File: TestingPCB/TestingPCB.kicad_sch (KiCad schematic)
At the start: 19 parts, among them J1 Conn_01x04, J2 USB_C_Receptacle_USB2.0_14P, J4 Conn_01x10, U1 SC0915, U2 CP2102N-Axx-xQFN24, U3 USBLC6-2P6

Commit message: Updated to use the 20 pin package and fixed power for CP2102N
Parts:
- removed U2: CP2102N-Axx-xQFN24, Package_DFN_QFN:QFN-24-1EP_4x4mm_P0.5mm_EP2.6x2.6mm, symbol Interface_USB:CP2102N-Axx-xQFN24
- added U4: CP2102N-Axx-xQFN20, Package_DFN_QFN:SiliconLabs_QFN-20-1EP_3x3mm_P0.5mm_EP1.8x1.8mm, symbol Interface_USB:CP2102N-Axx-xQFN20
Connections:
- net 3.3V: no longer C3.1, C4.1, R5.1
- net D_N: now also U4.5 (D-)
- net D_P: now also U4.4 (D+)
- net GND: now also U4.12 (GND), U4.21 (GND), U4.3 (GND)
- net RX: now also U4.18 (TXD)
- net TX: now also U4.17 (RXD)
- net USB 5V: now also U4.7 (VREGIN)
- net at R3.2, R4.1: now also U4.8 (VBUS)
- net at R5.2: now also U4.9 (~{RST})
- new net VDD: C3.1, C4.1, R5.1, U4.6 (VDD)
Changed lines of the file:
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@@
 	(title_block
 		(title "Thesis PCB")
-		(date "2025-03-09")
+		(date "2025-03-10")
 		(rev "v1.0")
 		(company "Lafayette College Electrical & Computer Engineering Department")
@@
 	)
 	(junction
-		(at 85.09 100.33)
-		(diameter 0)
-		(color 0 0 0 0)
-	)
-	(junction
 		(at 73.66 31.75)
 		(diameter 0)
@@
 	)
 	(junction
+		(at 83.82 93.98)
+		(diameter 0)
+		(color 0 0 0 0)
+	)
+	(junction
 		(at 119.38 81.28)
 		(diameter 0)
@@
 	(wire
 		(pts
-			(xy 83.82 104.14) (xy 83.82 100.33)
-		)
-		(stroke
-			(width 0)
-			(type default)
-		)
-	)
-	(wire
-		(pts
 			(xy 259.08 125.73) (xy 259.08 123.19)
 		)
@@
 	(wire
 		(pts
-			(xy 85.09 100.33) (xy 86.36 100.33)
+			(xy 83.82 93.98) (xy 115.57 93.98)
 		)
 		(stroke
@@
 	(wire
 		(pts
-			(xy 85.09 93.98) (xy 85.09 100.33)
-		)
-		(stroke
-			(width 0)
-			(type default)
-		)
-	)
-	(wire
-		(pts
 			(xy 132.08 115.57) (xy 132.08 106.68)
 		)
@@
 	(wire
 		(pts
-			(xy 86.36 100.33) (xy 86.36 104.14)
-		)
-		(stroke
-			(width 0)
-			(type default)
-		)
-	)
-	(wire
-		(pts
 			(xy 115.57 93.98) (xy 115.57 99.06)
 		)
@@
 	(wire
 		(pts
-			(xy 83.82 100.33) (xy 85.09 100.33)
-		)
-		(stroke
-			(width 0)
-			(type default)
-		)
-	)
-	(wire
-		(pts
 			(xy 156.21 46.99) (xy 165.1 46.99)
 		)
@@
 	(wire
 		(pts
+			(xy 83.82 93.98) (xy 83.82 104.14)
+		)
+		(stroke
+			(width 0)
+			(type default)
+		)
+	)
+	(wire
+		(pts
 			(xy 53.34 44.45) (xy 53.34 45.72)
 		)
@@
 	(wire
 		(pts
-			(xy 85.09 93.98) (xy 115.57 93.98)
-		)
-		(stroke
-			(width 0)
-			(type default)
-		)
-	)
-	(wire
-		(pts
 			(xy 254 130.81) (xy 259.08 130.81)
 		)
@@
 		(pts
 			(xy 46.99 43.18) (xy 53.34 43.18)
+		)
+		(stroke
+			(width 0)
+			(type default)
+		)
+	)
+	(wire
+		(pts
+			(xy 83.82 87.63) (xy 83.82 93.98)
 		)
 		(stroke
@@
 		)
 	)
-	(label "3.3V"
-		(at 124.46 93.98 0)
-		(effects
-			(font
-				(size 1.27 1.27)
-			)
-			(justify left bottom)
-		)
-	)
 	(label "5V"
 		(at 165.1 25.4 0)
@@
 		)
 	)
+	(label "VDD"
+		(at 66.04 87.63 0)
+		(effects
+			(font
+				(size 1.27 1.27)
+			)
+			(justify left bottom)
+		)
+	)
 	(label "GND"
 		(at 119.38 85.09 0)
@@
 		)
 	)
+	(label "VDD"
+		(at 83.82 87.63 0)
+		(effects
+			(font
+				(size 1.27 1.27)
+			)
+			(justify left bottom)
+		)
+	)
 	(label "GND"
 		(at 83.82 165.1 0)
@@
 	(label "GND"
 		(at 31.75 68.58 0)
-		(effects
-			(font
-				(size 1.27 1.27)
-			)
-			(justify left bottom)
-		)
-	)
-	(label "3.3V"
-		(at 66.04 87.63 0)
 		(effects
 			(font
@@
 	)
 	(symbol
-		(lib_id "Interface_USB:CP2102N-Axx-xQFN24")
-		(at 83.82 132.08 0)
-		(unit 1)
-		(exclude_from_sim no)
-		(in_bom yes)
-		(on_board yes)
-		(dnp no)
-		(fields_autoplaced yes)
-		(property "Reference" "U2"
-			(at 86.0141 160.02 0)
-			(effects
-				(font
-					(size 1.27 1.27)
-				)
-				(justify left)
-			)
-		)
-		(property "Value" "CP2102N-Axx-xQFN24"
-			(at 86.0141 162.56 0)
-			(effects
-				(font
-					(size 1.27 1.27)
-				)
-				(justify left)
-			)
-		)
-		(property "Footprint" "Package_DFN_QFN:QFN-24-1EP_4x4mm_P0.5mm_EP2.6x2.6mm"
-			(at 115.57 158.75 0)
-			(effects
-				(font
-					(size 1.27 1.27)
-				)
-				(hide yes)
-			)
-		)
-		(property "Datasheet" "https://www.silabs.com/documents/public/data-sheets/cp2102n-datasheet.pdf"
-			(at 85.09 151.13 0)
-			(effects
-				(font
-					(size 1.27 1.27)
-				)
-				(hide yes)
-			)
-		)
-		(property "Description" "USB to UART master bridge, QFN-24"
-			(at 83.82 132.08 0)
-			(effects
-				(font
-					(size 1.27 1.27)
-				)
-				(hide yes)
-			)
-		)
-		(property "Manufacturer Part Number" "CP2102N-A02-GQFN24R"
-			(at 83.82 132.08 0)
-			(effects
-				(font
-					(size 1.27 1.27)
-				)
-				(hide yes)
-			)
-		)
-		(pin "19"
-		)
-		(pin "25"
-		)
-		(pin "3"
-		)
-		(pin "20"
-		)
-		(pin "21"
-		)
-		(pin "12"
-		)
-		(pin "18"
-		)
-		(pin "2"
-		)
-		(pin "10"
-		)
-		(pin "17"
-		)
-		(pin "24"
-		)
-		(pin "4"
-		)
-		(pin "5"
-		)
-		(pin "8"
-		)
-		(pin "9"
-		)
-		(pin "6"
-		)
-		(pin "7"
-		)
-		(pin "22"
-		)
-		(pin "23"
-		)
-		(pin "14"
-		)
-		(pin "13"
-		)
-		(pin "15"
-		)
-		(pin "16"
-		)
-		(pin "11"
-		)
-		(pin "1"
-		)
-		(instances
-			(project ""
-				(path "/8bb8fabd-08ec-4863-9d8b-dc20b6f396de"
-					(reference "U2")
-					(unit 1)
-				)
-			)
-		)
-	)
-	(symbol
 		(lib_id "Device:C")
 		(at 115.57 102.87 0)
@@
 					(unit 1)
 				)
+			)
+		)
+	)
+	(symbol
+		(lib_id "Interface_USB:CP2102N-Axx-xQFN20")
+		(at 83.82 132.08 0)
+		(unit 1)
+		(exclude_from_sim no)
+		(in_bom yes)
+		(on_board yes)
+		(dnp no)
+		(fields_autoplaced yes)
+		(property "Reference" "U4"
+			(at 86.0141 160.02 0)
+			(effects
+				(font
+					(size 1.27 1.27)
+				)
+				(justify left)
+			)
+		)
+		(property "Value" "CP2102N-Axx-xQFN20"
+			(at 86.0141 162.56 0)
+			(effects
+				(font
+					(size 1.27 1.27)
+				)
+				(justify left)
+			)
+		)
+		(property "Footprint" "Package_DFN_QFN:SiliconLabs_QFN-20-1EP_3x3mm_P0.5mm_EP1.8x1.8mm"
+			(at 115.57 158.75 0)
+			(effects
+				(font
+					(size 1.27 1.27)
+				)
+				(hide yes)
+			)
+		)
+		(property "Datasheet" "https://www.silabs.com/documents/public/data-sheets/cp2102n-datasheet.pdf"
+			(at 85.09 151.13 0)
+			(effects
+				(font
+					(size 1.27 1.27)
+				)
+				(hide yes)
+			)
+		)
+		(property "Description" "USB to UART master bridge, QFN-20"
+			(at 83.82 132.08 0)
+			(effects
+				(font
+					(size 1.27 1.27)
+				)
+				(hide yes)
+			)
+		)
+		(pin "18"
+		)
+		(pin "13"
+		)
+		(pin "14"
+		)
+		(pin "17"
+		)
+		(pin "11"
+		)
+		(pin "8"
+		)
+		(pin "9"
+		)
+		(pin "6"
+		)
+		(pin "7"
+		)
+		(pin "4"
+		)
+		(pin "5"
+		)
+		(pin "2"
+		)
+		(pin "20"
+		)
+		(pin "21"
+		)
+		(pin "3"
+		)
+		(pin "15"
+		)
+		(pin "10"
+		)
+		(pin "1"
+		)
+		(pin "16"
+		)
+		(pin "12"
+		)
+		(pin "19"
+		)
+		(instances
+			(project ""
+				(path "/8bb8fabd-08ec-4863-9d8b-dc20b6f396de"
+					(reference "U4")
+					(unit 1)
+				)

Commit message: Updated BOM
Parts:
- J4: Manufacturer Part Number (none) -> M20-8891045
- U4: Manufacturer Part Number (none) -> CP2102N-A02-GQFN20R
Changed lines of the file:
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@@
+			)
+		)
+		(property "Manufacturer Part Number" "M20-8891045"
+			(at 151.13 57.15 0)
+			(effects
+				(font
+					(size 1.27 1.27)
+				)
+				(hide yes)
 			)
 		)
@@
 			(at 83.82 132.08 0)
 			(effects
+				(font
+					(size 1.27 1.27)
+				)
+				(hide yes)
+			)
+		)
+		(property "Manufacturer Part Number" "CP2102N-A02-GQFN20R"
+			(at 83.82 132.08 0)
+			(effects

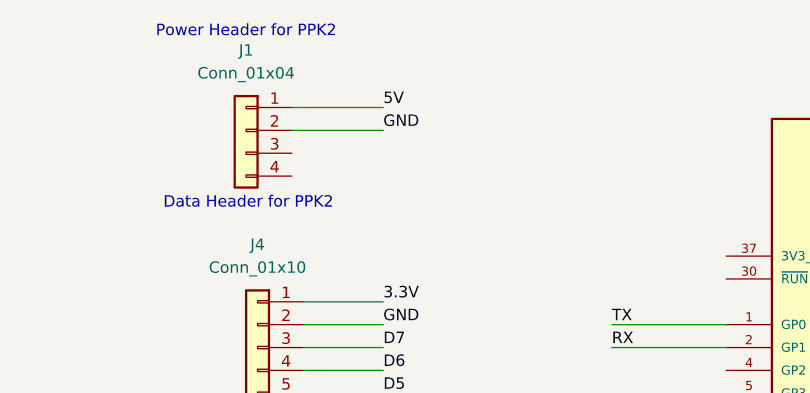
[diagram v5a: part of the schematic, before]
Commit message: Fixed power pinout
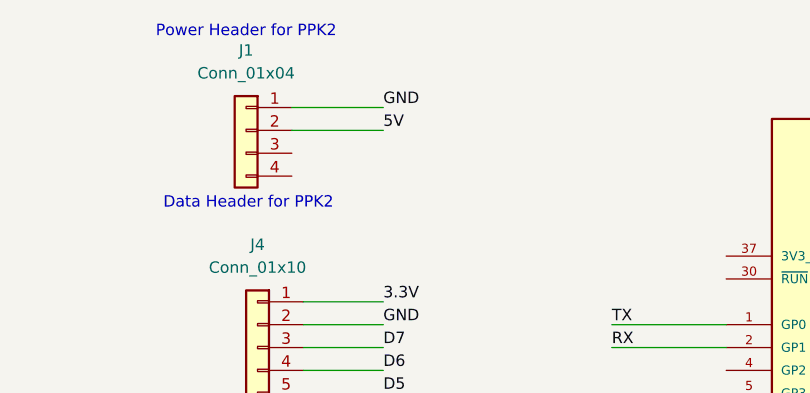
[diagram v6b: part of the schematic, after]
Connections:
- net 5V: now also J1.2 (Pin_2); no longer J1.1 (Pin_1)
- net GND: now also J1.1 (Pin_1); no longer J1.2 (Pin_2)
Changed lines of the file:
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@@
 	(title_block
 		(title "Thesis PCB")
-		(date "2025-03-10")
-		(rev "v1.0")
+		(date "2025-04-08")
+		(rev "v1.1")
 		(company "Lafayette College Electrical & Computer Engineering Department")
 		(comment 1 "By Robbie Leslie")
@@
 	(wire
 		(pts
+			(xy 74.93 44.45) (xy 74.93 43.18)
+		)
+		(stroke
+			(width 0)
+			(type default)
+		)
+	)
+	(wire
+		(pts
+			(xy 57.15 30.48) (xy 57.15 27.94)
+		)
+		(stroke
+			(width 0)
+			(type default)
+		)
+	)
+	(wire
+		(pts
+			(xy 254 62.23) (xy 262.89 62.23)
+		)
+		(stroke
+			(width 0)
+			(type default)
+		)
+	)
+	(wire
+		(pts
+			(xy 254 118.11) (xy 259.08 118.11)
+		)
+		(stroke
+			(width 0)
+			(type default)
+		)
+	)
+	(wire
+		(pts
+			(xy 119.38 81.28) (xy 127 81.28)
+		)
+		(stroke
+			(width 0)
+			(type default)
+		)
+	)
+	(wire
+		(pts
+			(xy 46.99 40.64) (xy 53.34 40.64)
+		)
+		(stroke
+			(width 0)
+			(type default)
+		)
+	)
+	(wire
+		(pts
 			(xy 154.94 25.4) (xy 165.1 25.4)
 		)
@@
 	(wire
 		(pts
-			(xy 74.93 44.45) (xy 74.93 43.18)
-		)
-		(stroke
-			(width 0)
-			(type default)
-		)
-	)
-	(wire
-		(pts
-			(xy 57.15 30.48) (xy 57.15 27.94)
-		)
-		(stroke
-			(width 0)
-			(type default)
-		)
-	)
-	(wire
-		(pts
-			(xy 254 62.23) (xy 262.89 62.23)
-		)
-		(stroke
-			(width 0)
-			(type default)
-		)
-	)
-	(wire
-		(pts
-			(xy 254 118.11) (xy 259.08 118.11)
-		)
-		(stroke
-			(width 0)
-			(type default)
-		)
-	)
-	(wire
-		(pts
-			(xy 119.38 81.28) (xy 127 81.28)
-		)
-		(stroke
-			(width 0)
-			(type default)
-		)
-	)
-	(wire
-		(pts
-			(xy 46.99 40.64) (xy 53.34 40.64)
-		)
-		(stroke
-			(width 0)
-			(type default)
-		)
-	)
-	(wire
-		(pts
 			(xy 156.21 69.85) (xy 165.1 69.85)
 		)
@@
 	(wire
 		(pts
+			(xy 124.46 115.57) (xy 124.46 119.38)
+		)
+		(stroke
+			(width 0)
+			(type default)
+		)
+	)
+	(wire
+		(pts
+			(xy 259.08 128.27) (xy 259.08 130.81)
+		)
+		(stroke
+			(width 0)
+			(type default)
+		)
+	)
+	(wire
+		(pts
 			(xy 154.94 27.94) (xy 165.1 27.94)
-		)
-		(stroke
-			(width 0)
-			(type default)
-		)
-	)
-	(wire
-		(pts
-			(xy 124.46 115.57) (xy 124.46 119.38)
-		)
-		(stroke
-			(width 0)
-			(type default)
-		)
-	)
-	(wire
-		(pts
-			(xy 259.08 128.27) (xy 259.08 130.81)
 		)
 		(stroke
@@
 	)
 	(label "5V"
-		(at 165.1 25.4 0)
+		(at 165.1 27.94 0)
 		(effects
 			(font
@@
 	)
 	(label "GND"
-		(at 165.1 27.94 0)
+		(at 165.1 25.4 0)
 		(effects
 			(font
